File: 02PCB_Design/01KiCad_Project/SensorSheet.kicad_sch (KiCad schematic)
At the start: 14 parts, among them J1 MTSW-104-22-L-D-265-RA, U1 AS5047P-ATSM, U2 ISM330BXTR

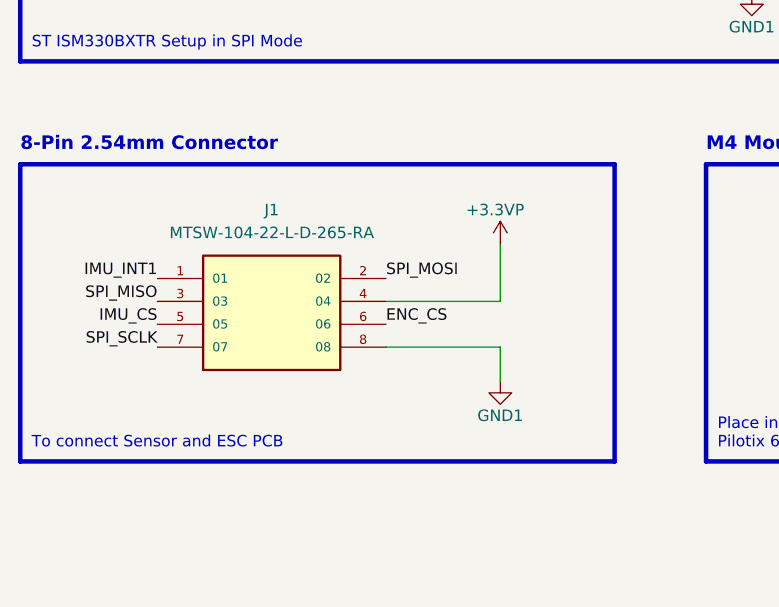
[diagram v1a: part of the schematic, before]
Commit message: sensor sheet & Power delivery
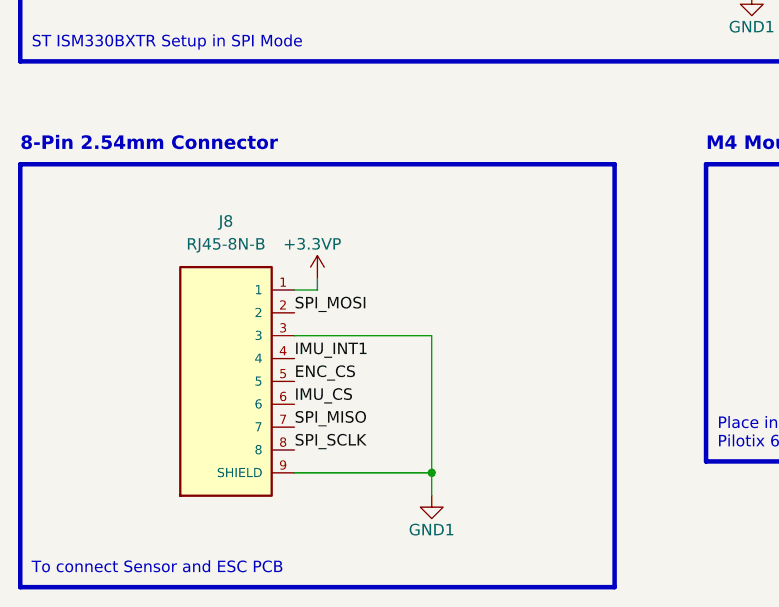
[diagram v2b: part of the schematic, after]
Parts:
- removed J1: MTSW-104-22-L-D-265-RA, Connector_PinHeader_2.54mm:PinHeader_2x04_P2.54mm_Horizontal, symbol MTSW-104-22-L-D-265-RA:MTSW-104-22-L-D-265-RA
- added J8: RJ45-8N-B, RJ45-8N-B:TE_RJ45-8N-B, symbol RJ45-8N-B:RJ45-8N-B
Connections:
- net +3.3VP: now also J8.1
- net ENC_CS: now also J8.5
- net GND1: now also J8.10 (SHIELD), J8.3, J8.9 (SHIELD)
- net IMU_CS: now also J8.6
- net IMU_INT1: now also J8.4
- net SPI_MISO: now also J8.7
- net SPI_MOSI: now also J8.2
- net SPI_SCLK: now also J8.8

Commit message: All Signals Connected, Ethernet Cable
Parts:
- renumbered J8 to J1
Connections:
- net ENC_CS: now also J1.8; no longer J1.5
- net IMU_CS: now also J1.4; no longer J1.6
- net IMU_INT1: now also J1.5; no longer J1.4
- net SPI_MISO: now also J1.6; no longer J1.7
- net SPI_SCLK: now also J1.7; no longer J1.8
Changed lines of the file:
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@@
     (effects (font (size 1.27 1.27)) (justify right bottom))
   )
-  (label "IMU_INT1" (at 73.66 134.62 0) (fields_autoplaced)
+  (label "IMU_INT1" (at 73.66 137.16 0) (fields_autoplaced)
     (effects (font (size 1.27 1.27)) (justify left bottom))
   )
@@
     (effects (font (size 1.27 1.27)) (justify right bottom))
   )
-  (label "SPI_MISO" (at 73.66 142.24 0) (fields_autoplaced)
+  (label "SPI_MISO" (at 73.66 139.7 0) (fields_autoplaced)
     (effects (font (size 1.27 1.27)) (justify left bottom))
   )
@@
     (effects (font (size 1.27 1.27)) (justify right bottom))
   )
-  (label "SPI_SCLK" (at 73.66 144.78 0) (fields_autoplaced)
+  (label "SPI_SCLK" (at 73.66 142.24 0) (fields_autoplaced)
     (effects (font (size 1.27 1.27)) (justify left bottom))
   )
@@
     (effects (font (size 1.27 1.27)) (justify right bottom))
   )
-  (label "ENC_CS" (at 73.66 137.16 0) (fields_autoplaced)
-    (effects (font (size 1.27 1.27)) (justify left bottom))
-  )
-  (label "IMU_CS" (at 73.66 139.7 0) (fields_autoplaced)
+  (label "ENC_CS" (at 73.66 144.78 0) (fields_autoplaced)
+    (effects (font (size 1.27 1.27)) (justify left bottom))
+  )
+  (label "IMU_CS" (at 73.66 134.62 0) (fields_autoplaced)
     (effects (font (size 1.27 1.27)) (justify left bottom))
   )
@@
   (symbol (lib_id "RJ45-8N-B:RJ45-8N-B") (at 66.04 137.16 0) (unit 1)
     (in_bom yes) (on_board yes) (dnp no) (fields_autoplaced)
-    (property "Reference" "J8" (at 66.04 119.38 0)
+    (property "Reference" "J1" (at 66.04 119.38 0)
       (effects (font (size 1.27 1.27)))
     )
@@
       (project "Testplatine"
         (path "/de27a806-41f8-462d-8678-2476d523bbd9/0ea8859b-b4da-4255-ae22-5fc50d726aba"
-          (reference "J8") (unit 1)
-        )
-      )
+          (reference "J1") (unit 1)
+        )
+      )

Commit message: edited footprints
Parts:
- removed H1, H2, H3, H4: MountingHole, MountingHole:MountingHole_4.3mm_M4_Pad_Via, symbol Mechanical:MountingHole
- added H1, H2, H3: MountingHole_Pad, MountingHole:MountingHole_4.3mm_M4_Pad_Via, symbol Mechanical:MountingHole_Pad
- J1: footprint RJ45-8N-B:TE_RJ45-8N-B -> MyFootprintLib:Wurth_634008_RJ45
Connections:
- net ENC_CS: now also J1.7; no longer J1.8
- net GND1: now also J1.5, J1.SHIELD, H1.1, H2.1, H3.1; no longer J1.10 (SHIELD), J1.3, J1.9 (SHIELD)
- net IMU_INT1: now also J1.3; no longer J1.5
- net SPI_MISO: now also J1.8; no longer J1.6
- net SPI_SCLK: now also J1.6; no longer J1.7
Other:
- moved on the sheet: J1

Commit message: Edited some connectors
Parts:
- added C78: 10uF, Capacitor_SMD:C_1206_3216Metric_Pad1.33x1.80mm_HandSolder, symbol Device:C
- added C79: 100nF, Capacitor_SMD:C_0603_1608Metric_Pad1.08x0.95mm_HandSolder, symbol Device:C
- added D4: LED, LED_SMD:LED_0805_2012Metric_Pad1.15x1.40mm_HandSolder, symbol Device:LED
- added R46: 2.2k, Resistor_SMD:R_0805_2012Metric_Pad1.20x1.40mm_HandSolder, symbol Device:R
- J1: value RJ45-8N-B -> Wurth-634008
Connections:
- net +3.3VP: now also C78.1, C79.1, R46.1
- net GND1: now also C78.2, C79.2, D4.1 (K)
- new net: D4.2 (A), R46.2
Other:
- moved on the sheet: J1

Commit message: relayout in progress
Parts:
- C78: footprint Capacitor_SMD:C_1206_3216Metric_Pad1.33x1.80mm_HandSolder -> Capacitor_SMD:C_1210_3225Metric_Pad1.33x2.70mm_HandSolder
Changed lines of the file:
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@@
       (effects (font (size 1.27 1.27)) (justify left))
     )
-    (property "Footprint" "Capacitor_SMD:C_1206_3216Metric_Pad1.33x1.80mm_HandSolder" (at 77.1652 133.35 0)
+    (property "Footprint" "Capacitor_SMD:C_1210_3225Metric_Pad1.33x2.70mm_HandSolder" (at 77.1652 133.35 0)
       (effects (font (size 1.27 1.27)) hide)
     )
